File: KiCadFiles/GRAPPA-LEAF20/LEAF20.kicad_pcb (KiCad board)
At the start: 2 copper layers, 234 x 44.5 mm, 48 parts

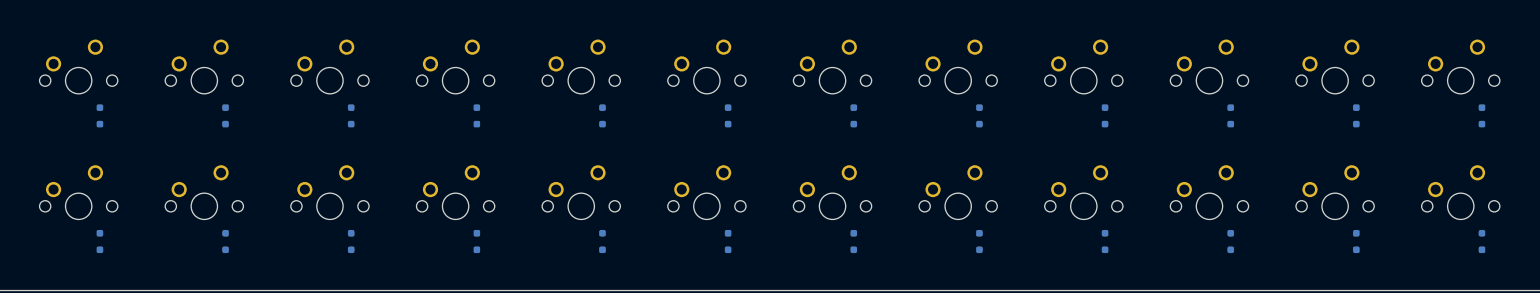
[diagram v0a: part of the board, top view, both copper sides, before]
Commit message: Add new KiCad project files for RC-2XXA, including PCB, schematic, and project files. Update existing schematic for RC-2XXX to adjust paper size and reposition components.
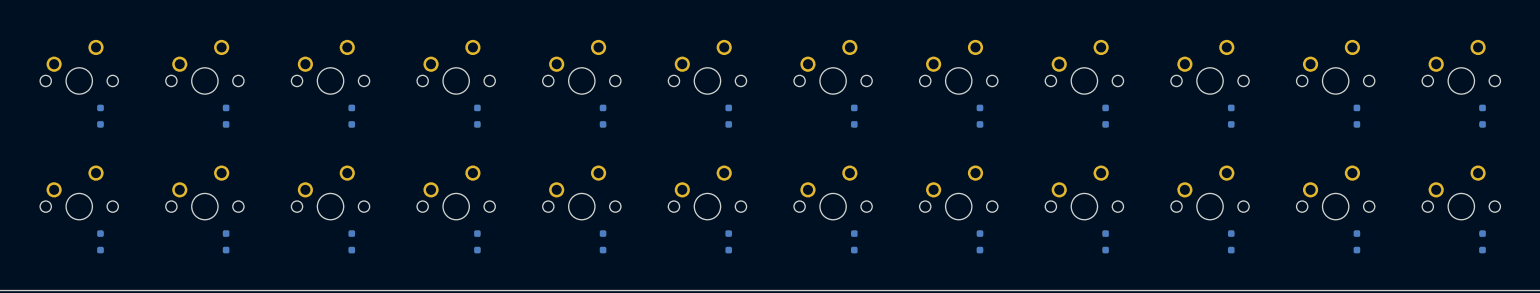
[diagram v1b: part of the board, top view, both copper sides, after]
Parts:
- moved D15 0.10 mm to (85.4, 60.2)
- moved D16 0.10 mm to (104.4, 60.2)
- moved D18 0.10 mm to (142.5, 60.2)
- moved D19 0.10 mm to (161.6, 60.2)
- moved D21 0.10 mm to (199.7, 60.2)
- moved D22 0.10 mm to (218.7, 60.2)
- moved D23 0.10 mm to (237.8, 60.2)
- moved MX15 0.10 mm to (82.2, 54.9)
- moved MX16 0.10 mm to (101.2, 54.9)
- moved MX18 0.10 mm to (139.3, 54.9)
- moved MX19 0.10 mm to (158.4, 54.9)
- moved MX21 0.10 mm to (196.5, 54.9)
- moved MX23 0.10 mm to (234.6, 54.9)
- moved MX24 0.10 mm to (253.6, 54.9)
- moved D10 0.10 mm to (218.7, 41.2)
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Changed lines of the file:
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@@
 	(footprint "My-Fi Footprints:SW_MX_1u"
 		(layer "F.Cu")
-		(at 139.23 35.77)
+		(at 139.315 35.815)
 		(descr "Footprint for Cherry MX style switches")
 		(tags "cherry mx switch")
@@
 	(footprint "My-Fi Footprints:SW_MX_1u"
 		(layer "F.Cu")
-		(at 139.23 54.82)
+		(at 139.315 54.865)
 		(descr "Footprint for Cherry MX style switches")
 		(tags "cherry mx switch")
@@
 	(footprint "My-Fi Footprints:SW_MX_1u"
 		(layer "F.Cu")
-		(at 63.03 35.77)
+		(at 63.115 35.815)
 		(descr "Footprint for Cherry MX style switches")
 		(tags "cherry mx switch")
@@
 	(footprint "My-Fi Footprints:SW_MX_1u"
 		(layer "F.Cu")
-		(at 43.98 35.77)
+		(at 44.065 35.815)
 		(descr "Footprint for Cherry MX style switches")
 		(tags "cherry mx switch")
@@
 	(footprint "My-Fi Footprints:SW_MX_1u"
 		(layer "F.Cu")
-		(at 101.13 35.77)
+		(at 101.215 35.815)
 		(descr "Footprint for Cherry MX style switches")
 		(tags "cherry mx switch")
@@
 	(footprint "My-Fi Footprints:SW_MX_1u"
 		(layer "F.Cu")
-		(at 101.13 54.82)
+		(at 101.215 54.865)
 		(descr "Footprint for Cherry MX style switches")
 		(tags "cherry mx switch")
@@
 	(footprint "My-Fi Footprints:SW_MX_1u"
 		(layer "F.Cu")
-		(at 158.28 35.77)
+		(at 158.365 35.815)
 		(descr "Footprint for Cherry MX style switches")
 		(tags "cherry mx switch")
@@
 	(footprint "My-Fi Footprints:SW_MX_1u"
 		(layer "F.Cu")
-		(at 253.53 35.77)
+		(at 253.615 35.815)
 		(descr "Footprint for Cherry MX style switches")
 		(tags "cherry mx switch")
@@
 	(footprint "My-Fi Footprints:SW_MX_1u"
 		(layer "F.Cu")
-		(at 177.33 35.77)
+		(at 177.415 35.815)
 		(descr "Footprint for Cherry MX style switches")
 		(tags "cherry mx switch")
@@
 	(footprint "My-Fi Footprints:SW_MX_1u"
 		(layer "F.Cu")
-		(at 196.38 35.77)
+		(at 196.465 35.815)
 		(descr "Footprint for Cherry MX style switches")
 		(tags "cherry mx switch")
@@
 	(footprint "My-Fi Footprints:SW_MX_1u"
 		(layer "F.Cu")
-		(at 177.33 54.82)
+		(at 177.415 54.865)
 		(descr "Footprint for Cherry MX style switches")
 		(tags "cherry mx switch")
@@
 	(footprint "My-Fi Footprints:SW_MX_1u"
 		(layer "F.Cu")
-		(at 82.08 35.77)
+		(at 82.165 35.815)
 		(descr "Footprint for Cherry MX style switches")
 		(tags "cherry mx switch")
@@
 	(footprint "My-Fi Footprints:SW_MX_1u"
 		(layer "F.Cu")
-		(at 120.18 35.77)
+		(at 120.265 35.815)
 		(descr "Footprint for Cherry MX style switches")
 		(tags "cherry mx switch")
@@
 	(footprint "My-Fi Footprints:SW_MX_1u"
 		(layer "F.Cu")
-		(at 63.03 54.82)
+		(at 63.115 54.865)
 		(descr "Footprint for Cherry MX style switches")
 		(tags "cherry mx switch")
@@
 	(footprint "My-Fi Footprints:SW_MX_1u"
 		(layer "F.Cu")
-		(at 234.48 54.82)
+		(at 234.565 54.865)
 		(descr "Footprint for Cherry MX style switches")
 		(tags "cherry mx switch")
@@
 	(footprint "My-Fi Footprints:SW_MX_1u"
 		(layer "F.Cu")
-		(at 253.53 54.82)
+		(at 253.615 54.865)
 		(descr "Footprint for Cherry MX style switches")
 		(tags "cherry mx switch")
@@
 	(footprint "My-Fi Footprints:SW_MX_1u"
 		(layer "F.Cu")
-		(at 158.28 54.82)
+		(at 158.365 54.865)
 		(descr "Footprint for Cherry MX style switches")
 		(tags "cherry mx switch")
@@
 	(footprint "My-Fi Footprints:SW_MX_1u"
 		(layer "F.Cu")
-		(at 215.43 35.77)
+		(at 215.515 35.815)
 		(descr "Footprint for Cherry MX style switches")
 		(tags "cherry mx switch")
@@
 	(footprint "My-Fi Footprints:SW_MX_1u"
 		(layer "F.Cu")
-		(at 120.18 54.82)
+		(at 120.265 54.865)
 		(descr "Footprint for Cherry MX style switches")
 		(tags "cherry mx switch")
@@
 	(footprint "My-Fi Footprints:SW_MX_1u"
 		(layer "F.Cu")
-		(at 43.98 54.82)
+		(at 44.065 54.865)
 		(descr "Footprint for Cherry MX style switches")
 		(tags "cherry mx switch")
@@
 	(footprint "My-Fi Footprints:SW_MX_1u"
 		(layer "F.Cu")
-		(at 215.43 54.82)
+		(at 215.515 54.865)
 		(descr "Footprint for Cherry MX style switches")
 		(tags "cherry mx switch")
@@
 	(footprint "My-Fi Footprints:SW_MX_1u"
 		(layer "F.Cu")
-		(at 234.48 35.77)
+		(at 234.565 35.815)
 		(descr "Footprint for Cherry MX style switches")
 		(tags "cherry mx switch")
@@
 	(footprint "My-Fi Footprints:SW_MX_1u"
 		(layer "F.Cu")
-		(at 82.08 54.82)
+		(at 82.165 54.865)
 		(descr "Footprint for Cherry MX style switches")
 		(tags "cherry mx switch")
@@
 	(footprint "My-Fi Footprints:SW_MX_1u"
 		(layer "F.Cu")
-		(at 196.38 54.82)
+		(at 196.465 54.865)
 		(descr "Footprint for Cherry MX style switches")
 		(tags "cherry mx switch")
@@
 	(footprint "Diode_SMD:D_SOD-323_HandSoldering"
 		(layer "B.Cu")
-		(at 104.35 60.159999 -90)
+		(at 104.435 60.204999 -90)
 		(descr "SOD-323")
 		(tags "SOD-323")
@@
 	(footprint "Diode_SMD:D_SOD-323_HandSoldering"
 		(layer "B.Cu")
-		(at 237.7 41.109999 -90)
+		(at 237.785 41.154999 -90)
 		(descr "SOD-323")
 		(tags "SOD-323")
@@
 	(footprint "Diode_SMD:D_SOD-323_HandSoldering"
 		(layer "B.Cu")
-		(at 142.45 41.109999 -90)
+		(at 142.535 41.154999 -90)
 		(descr "SOD-323")
 		(tags "SOD-323")
@@
 	(footprint "Diode_SMD:D_SOD-323_HandSoldering"
 		(layer "B.Cu")
-		(at 123.4 41.109999 -90)
+		(at 123.485 41.154999 -90)
 		(descr "SOD-323")
 		(tags "SOD-323")
@@
 	(footprint "Diode_SMD:D_SOD-323_HandSoldering"
 		(layer "B.Cu")
-		(at 199.6 41.109999 -90)
+		(at 199.685 41.154999 -90)
 		(descr "SOD-323")
 		(tags "SOD-323")
@@
 	(footprint "Diode_SMD:D_SOD-323_HandSoldering"
 		(layer "B.Cu")
-		(at 85.3 41.109999 -90)
+		(at 85.385 41.154999 -90)
 		(descr "SOD-323")
 		(tags "SOD-323")
@@
 	(footprint "Diode_SMD:D_SOD-323_HandSoldering"
 		(layer "B.Cu")
-		(at 142.45 60.159999 -90)
+		(at 142.535 60.204999 -90)
 		(descr "SOD-323")
 		(tags "SOD-323")
@@
 	(footprint "Diode_SMD:D_SOD-323_HandSoldering"
 		(layer "B.Cu")
-		(at 218.65 60.159999 -90)
+		(at 218.735 60.204999 -90)
 		(descr "SOD-323")
 		(tags "SOD-323")
@@
 	(footprint "Diode_SMD:D_SOD-323_HandSoldering"
 		(layer "B.Cu")
-		(at 180.55 41.109999 -90)
+		(at 180.635 41.154999 -90)
 		(descr "SOD-323")
 		(tags "SOD-323")
@@
 	(footprint "Diode_SMD:D_SOD-323_HandSoldering"
 		(layer "B.Cu")
-		(at 47.2 60.159999 -90)
+		(at 47.285 60.204999 -90)
 		(descr "SOD-323")
 		(tags "SOD-323")
@@
 	(footprint "Diode_SMD:D_SOD-323_HandSoldering"
 		(layer "B.Cu")
-		(at 256.75 41.109999 -90)
+		(at 256.835 41.154999 -90)
 		(descr "SOD-323")
 		(tags "SOD-323")
@@
 	(footprint "Diode_SMD:D_SOD-323_HandSoldering"
 		(layer "B.Cu")
-		(at 123.4 60.159999 -90)
+		(at 123.485 60.204999 -90)
 		(descr "SOD-323")
 		(tags "SOD-323")
@@
 	(footprint "Diode_SMD:D_SOD-323_HandSoldering"
 		(layer "B.Cu")
-		(at 199.6 60.159999 -90)
+		(at 199.685 60.204999 -90)
 		(descr "SOD-323")
 		(tags "SOD-323")
@@
 	(footprint "Diode_SMD:D_SOD-323_HandSoldering"
 		(layer "B.Cu")
-		(at 218.65 41.109999 -90)
+		(at 218.735 41.154999 -90)
 		(descr "SOD-323")
 		(tags "SOD-323")
@@
 	(footprint "Diode_SMD:D_SOD-323_HandSoldering"
 		(layer "B.Cu")
-		(at 104.35 41.109999 -90)
+		(at 104.435 41.154999 -90)
 		(descr "SOD-323")
 		(tags "SOD-323")
@@
 	(footprint "Diode_SMD:D_SOD-323_HandSoldering"
 		(layer "B.Cu")
-		(at 256.75 60.159999 -90)
+		(at 256.835 60.204999 -90)
 		(descr "SOD-323")
 		(tags "SOD-323")
@@
 	(footprint "Diode_SMD:D_SOD-323_HandSoldering"
 		(layer "B.Cu")
-		(at 180.55 60.159999 -90)
+		(at 180.635 60.204999 -90)
 		(descr "SOD-323")
 		(tags "SOD-323")
@@
 	(footprint "Diode_SMD:D_SOD-323_HandSoldering"
 		(layer "B.Cu")
-		(at 47.2 41.109999 -90)
+		(at 47.285 41.154999 -90)
 		(descr "SOD-323")
 		(tags "SOD-323")
@@
 	(footprint "Diode_SMD:D_SOD-323_HandSoldering"
 		(layer "B.Cu")
-		(at 161.5 41.109999 -90)
+		(at 161.585 41.154999 -90)
 		(descr "SOD-323")
 		(tags "SOD-323")
@@
 	(footprint "Diode_SMD:D_SOD-323_HandSoldering"
 		(layer "B.Cu")
-		(at 66.25 41.109999 -90)
+		(at 66.335 41.154999 -90)
 		(descr "SOD-323")
 		(tags "SOD-323")
@@
 	(footprint "Diode_SMD:D_SOD-323_HandSoldering"
 		(layer "B.Cu")
-		(at 161.5 60.159999 -90)
+		(at 161.585 60.204999 -90)
 		(descr "SOD-323")
 		(tags "SOD-323")
@@
 	(footprint "Diode_SMD:D_SOD-323_HandSoldering"
 		(layer "B.Cu")
-		(at 85.3 60.159999 -90)
+		(at 85.385 60.204999 -90)
 		(descr "SOD-323")
 		(tags "SOD-323")
@@
 	(footprint "Diode_SMD:D_SOD-323_HandSoldering"
 		(layer "B.Cu")
-		(at 237.7 60.159999 -90)
+		(at 237.785 60.204999 -90)
 		(descr "SOD-323")
 		(tags "SOD-323")
@@
 	(footprint "Diode_SMD:D_SOD-323_HandSoldering"
 		(layer "B.Cu")
-		(at 66.25 60.159999 -90)
+		(at 66.335 60.204999 -90)
 		(descr "SOD-323")
 		(tags "SOD-323")

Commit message: Refactor code structure for improved readability and maintainability
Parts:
- added J1: Conn_01x01_Pin, Connector_Wire:SolderWire-0.75sqmm_1x01_D1.25mm_OD2.3mm, B.Cu at (34.4, 25.7)
- added J4: Conn_01x08_Socket, Connector_JST:JST_SH_SM08B-SRSS-TB_1x08-1MP_P1.00mm_Horizontal, B.Cu at (72.1, 21.9)
- added J5: Conn_01x07_Socket, Connector_JST:JST_SH_SM07B-SRSS-TB_1x07-1MP_P1.00mm_Horizontal, B.Cu at (225.0, 21.9)
- D1, D10, D11, D12, D13, D14, D15, D16, D17, D18, D19, D2, D20, D21, D22, D23, D24, D3, D4, D5, D6, D7, D8, D9: footprint Diode_SMD:D_SOD-323_HandSoldering -> My-Fi Footprints:D_SOD-123-g
- moved D10 0.77 mm to (218.6, 40.4), turned to 90 degrees
- moved D22 0.77 mm to (218.6, 59.4), turned to 90 degrees
- moved D15 0.77 mm to (85.3, 59.4), turned to 90 degrees
- moved D16 0.77 mm to (104.3, 59.4), turned to 90 degrees
- moved D3 0.77 mm to (85.3, 40.4), turned to 90 degrees
- moved D4 0.77 mm to (104.3, 40.4), turned to 90 degrees
- moved D1 0.77 mm to (47.2, 40.4), turned to 90 degrees
- moved D11 0.77 mm to (237.7, 40.4), turned to 90 degrees
- moved D13 0.77 mm to (47.2, 59.4), turned to 90 degrees
- moved D14 0.77 mm to (66.2, 59.4), turned to 90 degrees
- moved D17 0.77 mm to (123.4, 59.4), turned to 90 degrees
- moved D18 0.77 mm to (142.4, 59.4), turned to 90 degrees
- moved D19 0.77 mm to (161.5, 59.4), turned to 90 degrees
- moved D2 0.77 mm to (66.2, 40.4), turned to 90 degrees
- moved D20 0.77 mm to (180.5, 59.4), turned to 90 degrees
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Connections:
- D1 pad 1: unconnected-(D1-K-Pad1) -> ROW0
- D10 pad 1: unconnected-(D10-K-Pad1) -> ROW0
- D11 pad 1: unconnected-(D11-K-Pad1) -> ROW0
- D12 pad 1: unconnected-(D12-K-Pad1) -> ROW0
- D13 pad 1: unconnected-(D13-K-Pad1) -> ROW1
- D14 pad 1: unconnected-(D14-K-Pad1) -> ROW1
- D15 pad 1: unconnected-(D15-K-Pad1) -> ROW1
- D16 pad 1: unconnected-(D16-K-Pad1) -> ROW1
- D17 pad 1: unconnected-(D17-K-Pad1) -> ROW1
- D18 pad 1: unconnected-(D18-K-Pad1) -> ROW1
- D19 pad 1: unconnected-(D19-K-Pad1) -> ROW1
- D2 pad 1: unconnected-(D2-K-Pad1) -> ROW0
- D20 pad 1: unconnected-(D20-K-Pad1) -> ROW1
- D21 pad 1: unconnected-(D21-K-Pad1) -> ROW1
- D22 pad 1: unconnected-(D22-K-Pad1) -> ROW1
- D23 pad 1: unconnected-(D23-K-Pad1) -> ROW1
- D24 pad 1: unconnected-(D24-K-Pad1) -> ROW1
- D3 pad 1: unconnected-(D3-K-Pad1) -> ROW0
- D4 pad 1: unconnected-(D4-K-Pad1) -> ROW0
- D5 pad 1: unconnected-(D5-K-Pad1) -> ROW0
- D6 pad 1: unconnected-(D6-K-Pad1) -> ROW0
- D7 pad 1: unconnected-(D7-K-Pad1) -> ROW0
- D8 pad 1: unconnected-(D8-K-Pad1) -> ROW0
- D9 pad 1: unconnected-(D9-K-Pad1) -> ROW0
- MX1 pad 1: unconnected-(MX1-Pad1) -> COL0
- MX10 pad 1: unconnected-(MX10-Pad1) -> COL9
- MX11 pad 1: unconnected-(MX11-Pad1) -> COL10
- MX12 pad 1: unconnected-(MX12-Pad1) -> COL11
- MX13 pad 1: unconnected-(MX13-Pad1) -> COL0
- MX14 pad 1: unconnected-(MX14-Pad1) -> COL1
- MX15 pad 1: unconnected-(MX15-Pad1) -> COL2
- MX16 pad 1: unconnected-(MX16-Pad1) -> COL3
- MX17 pad 1: unconnected-(MX17-Pad1) -> COL4
- MX18 pad 1: unconnected-(MX18-Pad1) -> COL5
- MX19 pad 1: unconnected-(MX19-Pad1) -> COL6
- MX2 pad 1: unconnected-(MX2-Pad1) -> COL1
- MX20 pad 1: unconnected-(MX20-Pad1) -> COL7
- MX21 pad 1: unconnected-(MX21-Pad1) -> COL8
- MX22 pad 1: unconnected-(MX22-Pad1) -> COL9
- MX23 pad 1: unconnected-(MX23-Pad1) -> COL10
- MX24 pad 1: unconnected-(MX24-Pad1) -> COL11
- MX3 pad 1: unconnected-(MX3-Pad1) -> COL2
- MX4 pad 1: unconnected-(MX4-Pad1) -> COL3
- MX5 pad 1: unconnected-(MX5-Pad1) -> COL4
- MX6 pad 1: unconnected-(MX6-Pad1) -> COL5
- MX7 pad 1: unconnected-(MX7-Pad1) -> COL6
- MX8 pad 1: unconnected-(MX8-Pad1) -> COL7
- MX9 pad 1: unconnected-(MX9-Pad1) -> COL8
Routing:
- net ROW1: track 0.00 -> 288.5 mm, vias 0 -> 2
- net ROW0: track 0.00 -> 270.1 mm
- net COL5: track 0.00 -> 110.5 mm
- net COL6: track 0.00 -> 92.7 mm
- net COL7: track 0.00 -> 75.2 mm
- net COL4: track 0.00 -> 65.5 mm
- net COL8: track 0.00 -> 57.5 mm
- net COL0: track 0.00 -> 56.2 mm
- net COL3: track 0.00 -> 47.4 mm
- net COL11: track 0.00 -> 46.8 mm
- net COL9: track 0.00 -> 39.9 mm
- net COL1: track 0.00 -> 39.6 mm
- net GND: track 0.00 -> 34.9 mm
- net COL2: track 0.00 -> 30.9 mm
- net COL10: track 0.00 -> 30.4 mm
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- added copper zone on B.Cu, net GND
- added copper zone on F.Cu, net GND
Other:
- board size 234 x 44.5 mm -> 234 x 49.5 mm
